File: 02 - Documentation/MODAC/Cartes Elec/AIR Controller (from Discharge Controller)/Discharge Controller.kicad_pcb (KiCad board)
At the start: 2 copper layers, 38.1 x 34.5 mm, 24 parts, among them J1 3P Droit 22-11-2032, J3 2P Droit 2-11-2022, K2 Relais PCB, Q1 NMOS SQ2348ES-T1_GE3, U1 Alim LP TSR_0.5-2450, U3 Opamp_Dual

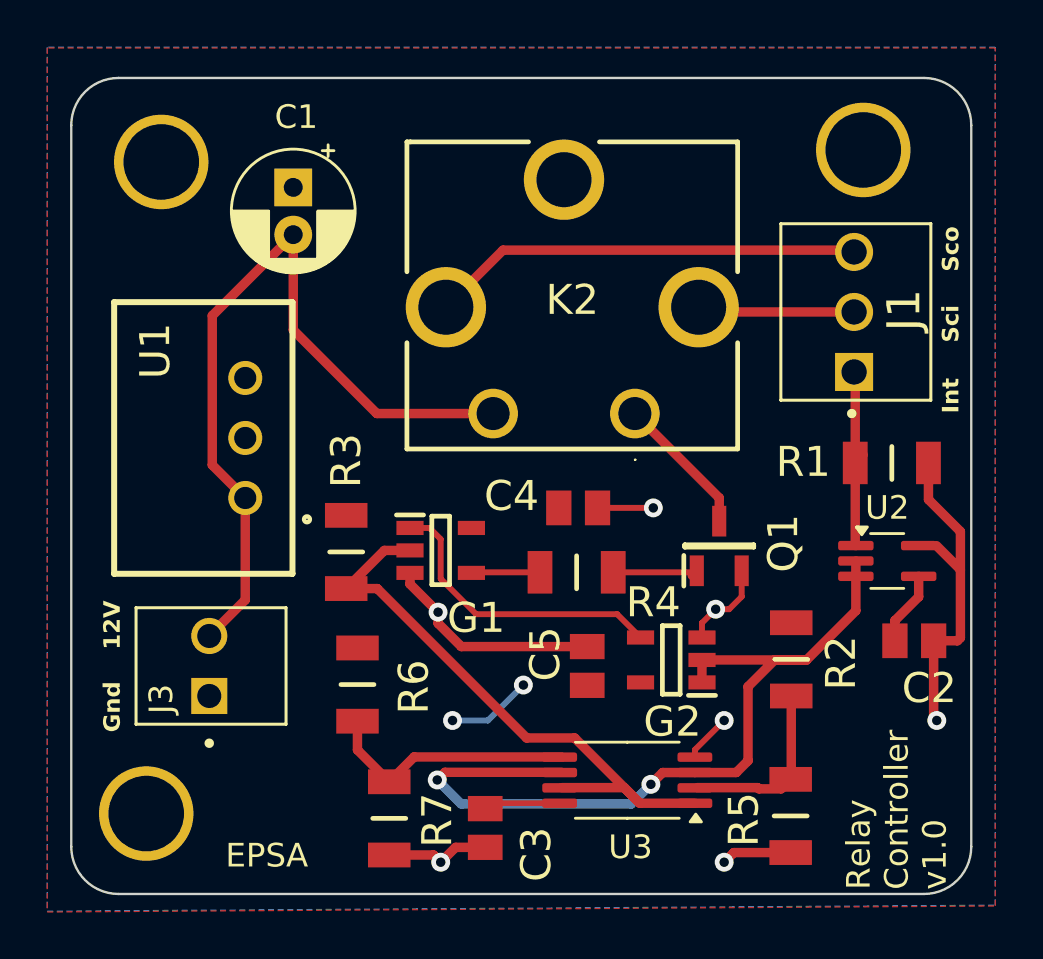
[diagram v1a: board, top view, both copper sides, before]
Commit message: Modif Discharge controller
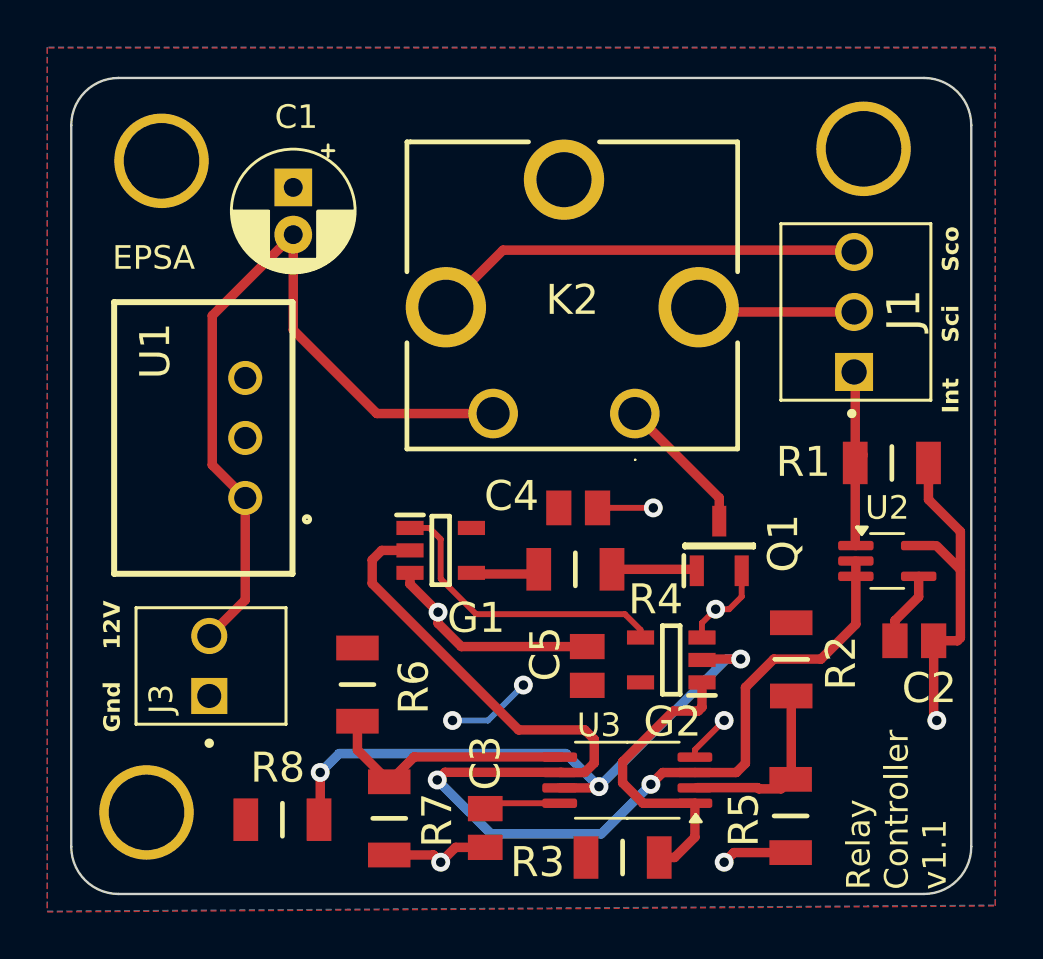
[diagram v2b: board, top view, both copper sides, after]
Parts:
- removed the ? at (153.0, 81.9)
- removed the ? at (153.7, 54.4)
- removed the ? at (183.4, 53.8)
- added ?: , , F.Cu at (153.0, 81.9)
- added ?: , , F.Cu at (183.4, 53.8)
- added ?: , , F.Cu at (153.7, 54.3)
- added R8: 10k, EPSA_lib:RESC3216X70N, F.Cu at (158.8, 82.2)
- moved R3 17.4 mm to (173.2, 83.8), turned to 0 degrees
- moved R4 0.14 mm to (171.2, 71.6)
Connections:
- G1 pad 2: /SCS_Compliance -> /Relay_Closed
- G2 pad 1: /Relay_Closed -> /SCS_Compliance_075
- G2 pad 2: /Relay_Closed -> /SCS_Compliance_425
- R3 pad 2: /SCS_Compliance -> /SCS_Compliance_075
- U3 pad 1: /SCS_Compliance -> /SCS_Compliance_075
- U3 pad 7: /SCS_Compliance -> /SCS_Compliance_425
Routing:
- net /SCS_Compliance_425: track 0.00 -> 26.3 mm, vias 0 -> 3
- net /SCS_Compliance: track 25.5 -> 0.00 mm
- net /Relay_Closed: track 36.3 -> 49.8 mm
- net /SCS_Compliance_075: track 0.00 -> 13.0 mm
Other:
- board text added: "Relay Controller v1.1"
- board text removed: "Relay Controller v1.0"

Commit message: Revert "Modif Discharge controller"
This reverts commit 299f52ab1fad389a0f7cf3a8ef8eeb6215b67b4a.
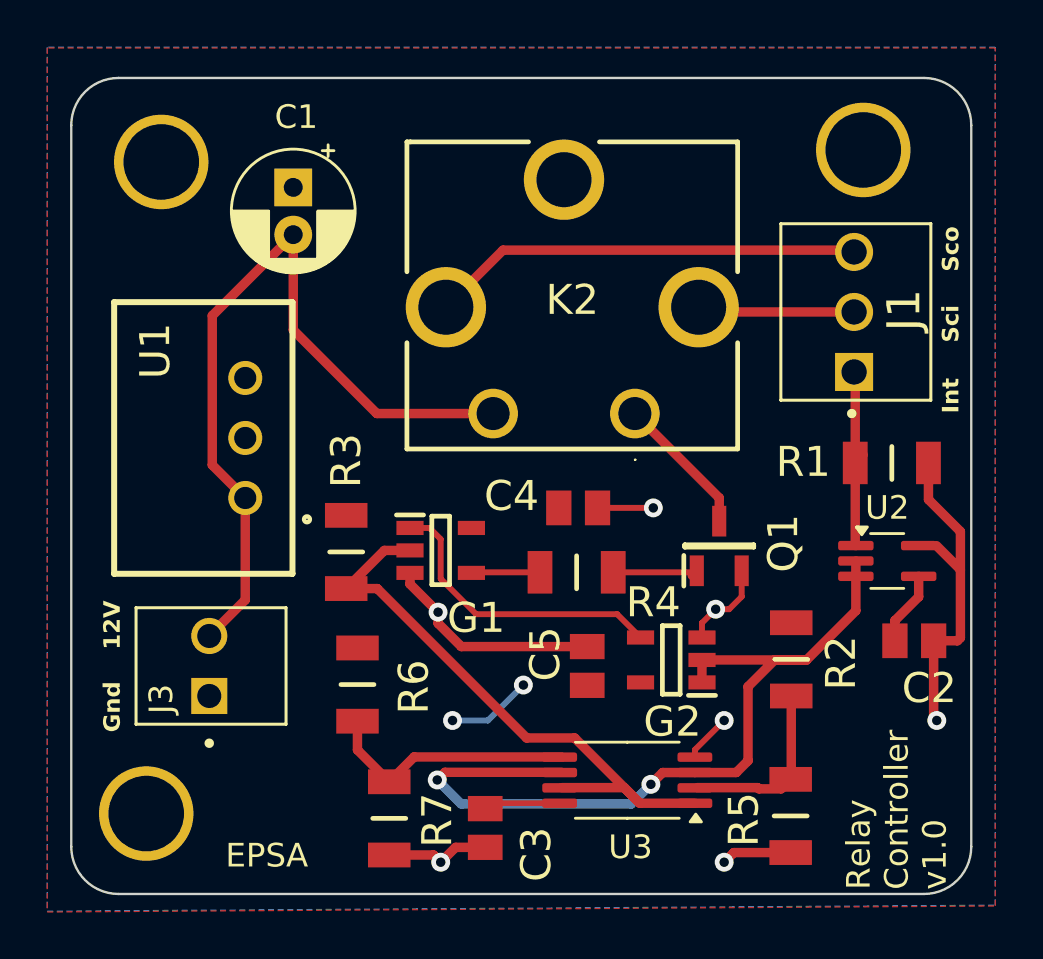
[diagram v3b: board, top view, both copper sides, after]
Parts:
- removed the ? at (153.0, 81.9)
- removed the ? at (183.4, 53.8)
- removed the ? at (153.7, 54.3)
- removed R8: 10k, EPSA_lib:RESC3216X70N
- added ?: , , F.Cu at (153.0, 81.9)
- added ?: , , F.Cu at (153.7, 54.4)
- added ?: , , F.Cu at (183.4, 53.8)
- moved R3 17.4 mm to (161.5, 70.9), turned to -90 degrees
- moved R4 0.14 mm to (171.3, 71.7)
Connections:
- G1 pad 2: /Relay_Closed -> /SCS_Compliance
- G2 pad 1: /SCS_Compliance_075 -> /Relay_Closed
- G2 pad 2: /SCS_Compliance_425 -> /Relay_Closed
- R3 pad 2: /SCS_Compliance_075 -> /SCS_Compliance
- U3 pad 1: /SCS_Compliance_075 -> /SCS_Compliance
- U3 pad 7: /SCS_Compliance_425 -> /SCS_Compliance
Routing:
- net /SCS_Compliance_425: track 26.3 -> 0.00 mm, vias 3 -> 0
- net /SCS_Compliance: track 0.00 -> 25.5 mm
- net /Relay_Closed: track 49.8 -> 36.3 mm
- net /SCS_Compliance_075: track 13.0 -> 0.00 mm
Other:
- board text added: "Relay Controller v1.0"
- board text removed: "Relay Controller v1.1"
